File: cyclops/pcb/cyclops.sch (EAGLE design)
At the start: 178 parts, among them Q4 IRF510, U1 MCP4921, U11 THS4281, U12 MAX4564, U13 ZXTD, U14 ZXTD, U15 OPA1664, U2 LT1931, U3 LT1764A, U31 TPS62153, U4 BD00IA5WEFJ-E2, U5 TPS72325, U6 LT1711, U7 TLV3701, U8 ADR03, U9 LT1880

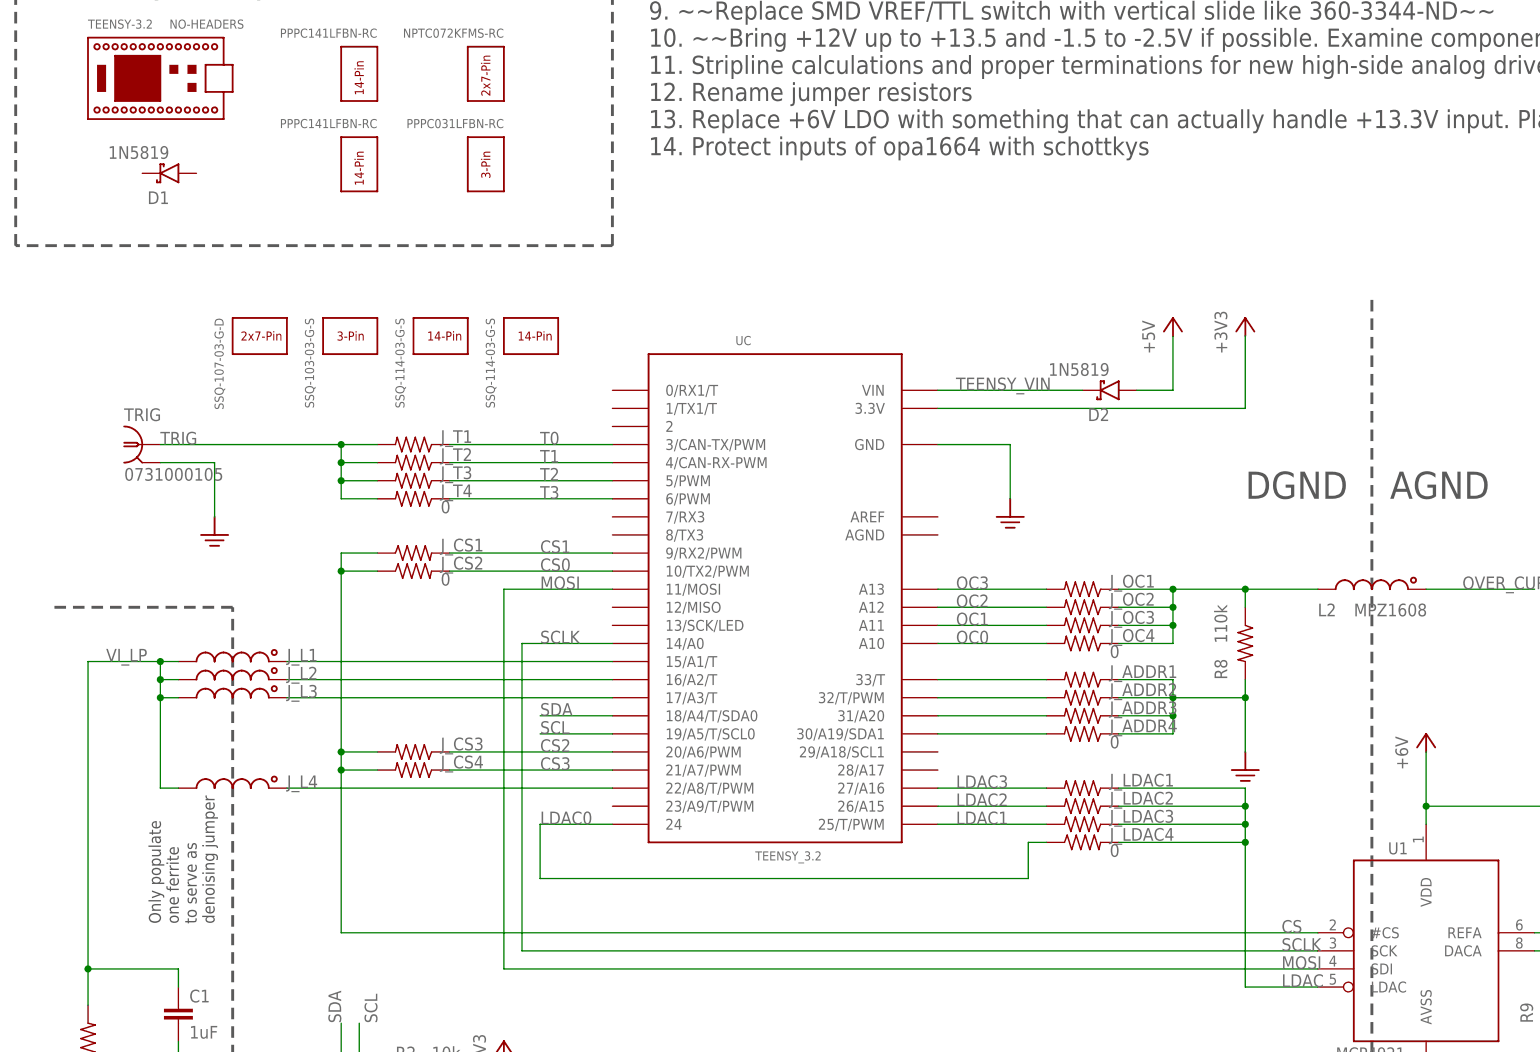
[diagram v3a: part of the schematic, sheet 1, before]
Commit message: Most digital layout is complete.
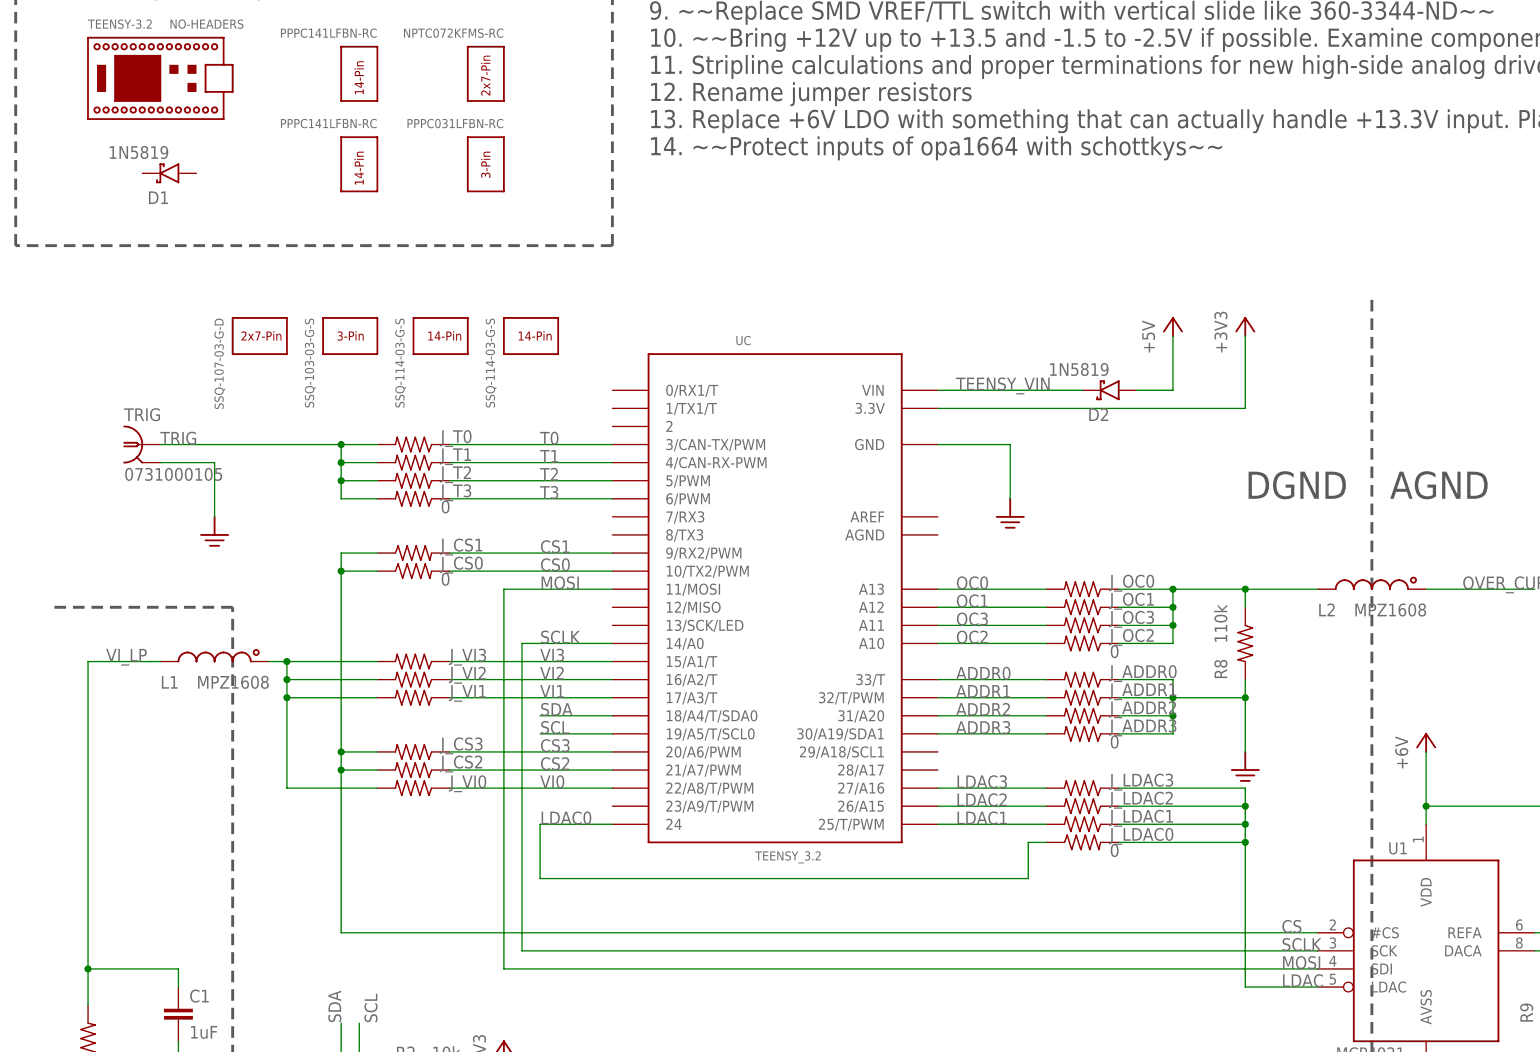
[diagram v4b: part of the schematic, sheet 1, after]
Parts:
- removed J_ADDR4, J_CS4, J_OC4, J_T4: 0, jonnew:R_0402
- removed J_L1, J_L2, J_L3, J_L4: MPZ1608, cyclops:L_0603
- added J_ADDR0, J_CS0, J_OC0, J_T0, J_VI0, J_VI1, J_VI2, J_VI3: 0, jonnew:R_0402
- added L1: MPZ1608, cyclops:L_0603
- renumbered J_LDAC4 to J_LDAC0
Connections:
- removed net N$19: J_L3.1, UC.17/A3/T
- removed net N$21: J_L2.1, UC.16/A2/T
- removed net N$23: J_L1.1, UC.15/A1/T
- removed net N$40: J_ADDR1.2, UC.33/T
- removed net N$41: J_ADDR2.2, UC.32/T/PWM
- removed net N$44: J_ADDR3.2, UC.31/A20
- removed net N$45: J_ADDR4.2, UC.30/A19/SDA1
- removed net N$7: J_L4.1, UC.22/A8/T/PWM
- new net ADDR0: J_ADDR0.2, UC.33/T
- new net ADDR1: J_ADDR1.2, UC.32/T/PWM
- new net ADDR2: J_ADDR2.2, UC.31/A20
- new net ADDR3: J_ADDR3.2, UC.30/A19/SDA1
- new net N$58: J_VI0.2, J_VI1.2, J_VI2.2, J_VI3.2, L1.1
- new net VI0: J_VI0.1, UC.22/A8/T/PWM
- new net VI1: J_VI1.1, UC.17/A3/T
- new net VI2: J_VI2.1, UC.16/A2/T
- new net VI3: J_VI3.1, UC.15/A1/T
- net CS: now also J_CS0.1, J_CS2.2; no longer J_CS2.1, J_CS4.2
- net CS0: now also J_CS0.2; no longer J_CS2.2
- net CS2: now also J_CS2.1, UC.21/A7/PWM; no longer J_CS3.1, UC.20/A6/PWM
- net CS3: now also J_CS3.1, UC.20/A6/PWM; no longer J_CS4.1, UC.21/A7/PWM
- net GND: now also J_ADDR0.1; no longer J_ADDR4.1
- net LDAC1: now also J_LDAC1.2; no longer J_LDAC3.2
- net LDAC3: now also J_LDAC3.2; no longer J_LDAC1.2
- net N$38: now also J_OC0.1; no longer J_OC4.1
- net OC0: now also J_OC0.2, UC.A13; no longer J_OC4.2, UC.A10
- net OC1: now also J_OC1.2, UC.A12; no longer J_OC3.2, UC.A11
- net OC2: now also UC.A10; no longer UC.A12
- net OC3: now also J_OC3.2, UC.A11; no longer J_OC1.2, UC.A13
- net OVER_CURR: now also U10.IN
- net T0: now also J_T0.1; no longer J_T1.1
- net T1: now also J_T1.1; no longer J_T2.1
- net T2: now also J_T2.1; no longer J_T3.1
- net T3: now also J_T3.1; no longer J_T4.1
- net TRIG: now also J_T0.2; no longer J_T4.2
- net VI_LP: now also L1.2; no longer J_L1.2, J_L2.2, J_L3.2, J_L4.2
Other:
- note removed: "Only populate one ferrite to serve as denoising jumper"
- moved on the sheet: J_ADDR1, J_ADDR2, J_ADDR3, J_CS2, J_LDAC1, J_LDAC3, J_OC1, J_OC2, J_T1, J_T2, J_T3

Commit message: Almost done with layout.
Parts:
- R10: device jonnew:R_0805 -> jonnew:R_0603
- R15: value 3k -> 2.2k
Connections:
- removed net N$38: J_OC0.1, J_OC1.1, J_OC2.1, J_OC3.1, L2.2, R8.1
- removed net V-: R20.2, U7G$2.V-, U9G$2.V-
- new net OVER_CURR_PRE: J_OC0.1, J_OC1.1, J_OC2.1, J_OC3.1, L2.2, R28.2, R8.1
- net GND: now also R20.2, U7G$2.V-, U9G$2.V-
- net OVER_CURR: no longer R28.2
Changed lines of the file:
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@@
 <part name="REF2V5" library="cyclops" deviceset="TP" device="TP16R" value="TPTP16R"/>
 <part name="REF5V0" library="cyclops" deviceset="TP" device="TP16R" value="TPTP16R"/>
-<part name="R15" library="cyclops" deviceset="R" device="_0603" value="3k"/>
+<part name="R15" library="cyclops" deviceset="R" device="_0603" value="2.2k"/>
 <part name="R20" library="cyclops" deviceset="R" device="_0603" value="10k"/>
 <part name="R17" library="cyclops" deviceset="R" device="_0603" value="40k"/>
@@
 <part name="U14" library="cyclops" deviceset="ZXTD4591E6" device="" value="ZXTD"/>
 <part name="SUPPLY14" library="cyclops" deviceset="+12V" device=""/>
-<part name="R10" library="jonnew" deviceset="R" device="_0805" value="100"/>
+<part name="R10" library="jonnew" deviceset="R" device="_0603" value="100"/>
 <part name="D3" library="cyclops" deviceset="Z-DIODE" device="_SOD-323" value="MM3Z5V1"/>
 <part name="U$21" library="cyclops" deviceset="GND2" device=""/>
@@
 </segment>
 </net>
-<net name="N$38" class="0">
+<net name="OVER_CURR_PRE" class="0">
 <segment>
 <wire x1="149.86" y1="101.6" x2="160.02" y2="101.6" width="0.1524" layer="91"/>
@@
 <wire x1="-43.18" y1="-45.72" x2="-43.18" y2="-48.26" width="0.1524" layer="91"/>
 </segment>
+<segment>
+<pinref part="U7" gate="G$2" pin="V-"/>
+<wire x1="-33.02" y1="60.96" x2="-33.02" y2="58.42" width="0.1524" layer="91"/>
+<pinref part="R20" gate="R" pin="2"/>
+<wire x1="-53.34" y1="58.42" x2="-53.34" y2="40.64" width="0.1524" layer="91"/>
+<wire x1="-33.02" y1="58.42" x2="-53.34" y2="58.42" width="0.1524" layer="91"/>
+<junction x="-53.34" y="58.42"/>
+<wire x1="-58.42" y1="58.42" x2="-53.34" y2="58.42" width="0.1524" layer="91"/>
+</segment>
 </net>
 <net name="N$5" class="0">
@@
 <wire x1="81.28" y1="93.98" x2="81.28" y2="88.9" width="0.1524" layer="91"/>
 <pinref part="OC" gate="2" pin="A"/>
-</segment>
-</net>
-<net name="OVER_CURR" class="0">
-<segment>
-<pinref part="R28" gate="R" pin="2"/>
-<wire x1="38.1" y1="68.58" x2="58.42" y2="68.58" width="0.1524" layer="91"/>
-<label x="38.1" y="68.58" size="1.778" layer="95"/>
 </segment>
 </net>
@@
 </segment>
 </net>
-<net name="V-" class="0">
-<segment>
-<pinref part="U7" gate="G$2" pin="V-"/>
-<wire x1="-33.02" y1="60.96" x2="-33.02" y2="58.42" width="0.1524" layer="91"/>
-<pinref part="R20" gate="R" pin="2"/>
-<wire x1="-53.34" y1="58.42" x2="-53.34" y2="40.64" width="0.1524" layer="91"/>
-<wire x1="-33.02" y1="58.42" x2="-53.34" y2="58.42" width="0.1524" layer="91"/>
-<junction x="-53.34" y="58.42"/>
-<wire x1="-58.42" y1="58.42" x2="-53.34" y2="58.42" width="0.1524" layer="91"/>
-</segment>
-</net>
 <net name="-2.5V" class="0">
 <segment>
@@
 <wire x1="-96.52" y1="58.42" x2="-116.84" y2="58.42" width="0.1524" layer="91"/>
 <label x="-116.84" y="58.42" size="1.778" layer="95"/>
+</segment>
+</net>
+<net name="OVER_CURR_PRE" class="0">
+<segment>
+<pinref part="R28" gate="R" pin="2"/>
+<wire x1="38.1" y1="68.58" x2="58.42" y2="68.58" width="0.1524" layer="91"/>
+<label x="38.1" y="68.58" size="1.778" layer="95"/>
 </segment>
 </net>
@@
 <wire x1="53.34" y1="-33.02" x2="53.34" y2="-73.66" width="0.1524" layer="91"/>
 </segment>
+<segment>
+<pinref part="U9" gate="G$2" pin="V-"/>
+<wire x1="5.08" y1="-35.56" x2="5.08" y2="-27.94" width="0.1524" layer="91"/>
+</segment>
 </net>
 <net name="N$6" class="0">
@@
 </segment>
 </net>
-<net name="V-" class="0">
-<segment>
-<pinref part="U9" gate="G$2" pin="V-"/>
-<wire x1="5.08" y1="-35.56" x2="5.08" y2="-27.94" width="0.1524" layer="91"/>
-</segment>
-</net>

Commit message: More routing. Very near completion.
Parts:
- removed C40: 10uF, jonnew:C_1206
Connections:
- net N$50 renamed ~LED_ACTIVE
- removed net N$48: D6.A
- removed net N$53: D5.C
- net +13.3V: no longer C40.1
- net +6V: now also D5.C
- net GND: now also D6.A; no longer C40.2
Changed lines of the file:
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@@
 <part name="U$2" library="cyclops" deviceset="GND2" device=""/>
 <part name="P+18" library="jonnew" deviceset="+5V" device="" value="+5V"/>
-<part name="C40" library="jonnew" deviceset="C" device="_1206" value="10uF"/>
 <part name="U31" library="jonnew" deviceset="TPS6125X" device="_VQFN16" value="TPS62153"/>
 <part name="L5" library="jonnew" deviceset="L" device="_4020" value="XFL4020-222ME"/>
@@
 <junction x="160.02" y="86.36"/>
 </segment>
+<segment>
+<pinref part="D6" gate="G$1" pin="A"/>
+<wire x1="20.32" y1="-63.5" x2="20.32" y2="-60.96" width="0.1524" layer="91"/>
+</segment>
 </net>
 <net name="VAUX" class="0">
@@
 <pinref part="C5" gate="C" pin="1"/>
 <wire x1="251.46" y1="71.12" x2="251.46" y2="45.72" width="0.1524" layer="91"/>
+</segment>
+<segment>
+<pinref part="D5" gate="G$1" pin="C"/>
+<wire x1="20.32" y1="-40.64" x2="20.32" y2="-38.1" width="0.1524" layer="91"/>
 </segment>
 </net>
@@
 <pinref part="R7" gate="R" pin="1"/>
 <wire x1="99.06" y1="-50.8" x2="101.6" y2="-50.8" width="0.1524" layer="91"/>
-</segment>
-</net>
-<net name="N$48" class="0">
-<segment>
-<pinref part="D6" gate="G$1" pin="A"/>
-<wire x1="20.32" y1="-63.5" x2="20.32" y2="-60.96" width="0.1524" layer="91"/>
-</segment>
-</net>
-<net name="N$53" class="0">
-<segment>
-<pinref part="D5" gate="G$1" pin="C"/>
-<wire x1="20.32" y1="-40.64" x2="20.32" y2="-38.1" width="0.1524" layer="91"/>
 </segment>
 </net>
@@
 <instance part="U4" gate="G$1" x="86.36" y="30.48"/>
 <instance part="P+18" gate="1" x="40.64" y="-33.02"/>
-<instance part="C40" gate="C" x="17.78" y="30.48"/>
 <instance part="U31" gate="G$1" x="-25.4" y="-50.8"/>
 <instance part="L5" gate="L" x="0" y="-38.1" rot="R270"/>
@@
 <pinref part="C10" gate="C" pin="-"/>
 <wire x1="-38.1" y1="-2.54" x2="-38.1" y2="-10.16" width="0.1524" layer="91"/>
-<pinref part="C40" gate="C" pin="2"/>
-<wire x1="17.78" y1="25.4" x2="17.78" y2="-2.54" width="0.1524" layer="91"/>
-<wire x1="17.78" y1="-2.54" x2="7.62" y2="-2.54" width="0.1524" layer="91"/>
-<junction x="7.62" y="-2.54"/>
 </segment>
 <segment>
@@
 <wire x1="27.94" y1="22.86" x2="27.94" y2="38.1" width="0.1524" layer="91"/>
 <junction x="7.62" y="38.1"/>
-<wire x1="7.62" y1="38.1" x2="17.78" y2="38.1" width="0.1524" layer="91"/>
-<wire x1="17.78" y1="38.1" x2="27.94" y2="38.1" width="0.1524" layer="91"/>
+<wire x1="7.62" y1="38.1" x2="27.94" y2="38.1" width="0.1524" layer="91"/>
 <wire x1="27.94" y1="38.1" x2="27.94" y2="45.72" width="0.1524" layer="91"/>
 <junction x="27.94" y="38.1"/>
 <pinref part="SUPPLY9" gate="G$1" pin="+12V"/>
-<pinref part="C40" gate="C" pin="1"/>
-<wire x1="17.78" y1="38.1" x2="17.78" y2="33.02" width="0.1524" layer="91"/>
-<junction x="17.78" y="38.1"/>
 <pinref part="C12" gate="C" pin="1"/>
 <pinref part="U4" gate="G$1" pin="EN"/>
@@
 </segment>
 </net>
-<net name="N$50" class="0">
+<net name="~LED_ACTIVE" class="0">
 <segment>
 <wire x1="-10.16" y1="-27.94" x2="-10.16" y2="-2.54" width="0.1524" layer="91"/>
@@
 <pinref part="U6" gate="G$1" pin="Q"/>
 <wire x1="-27.94" y1="-27.94" x2="-10.16" y2="-27.94" width="0.1524" layer="91"/>
-</segment>
-</net>
+<label x="-7.62" y="-27.94" size="1.778" layer="95" rot="R90"/>
+</segment>
+</net>

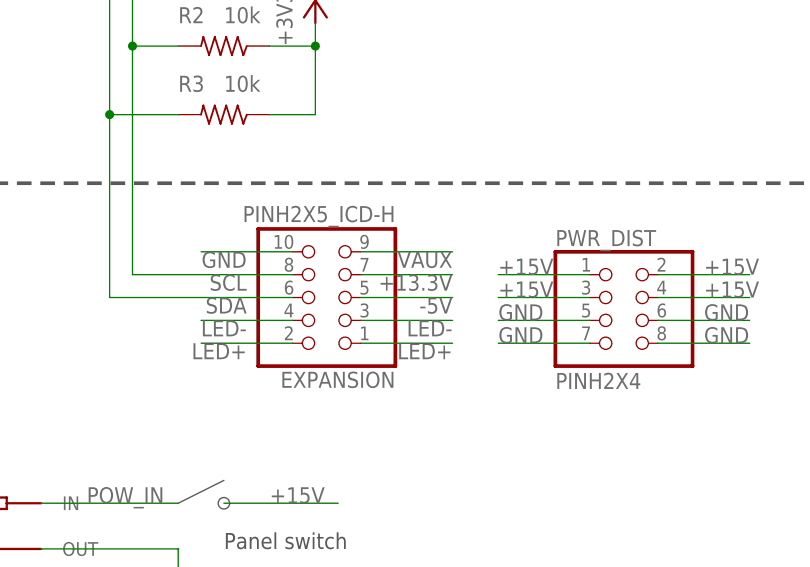
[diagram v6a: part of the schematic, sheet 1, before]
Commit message: More routing. Need to do ERC/DRC at this point.
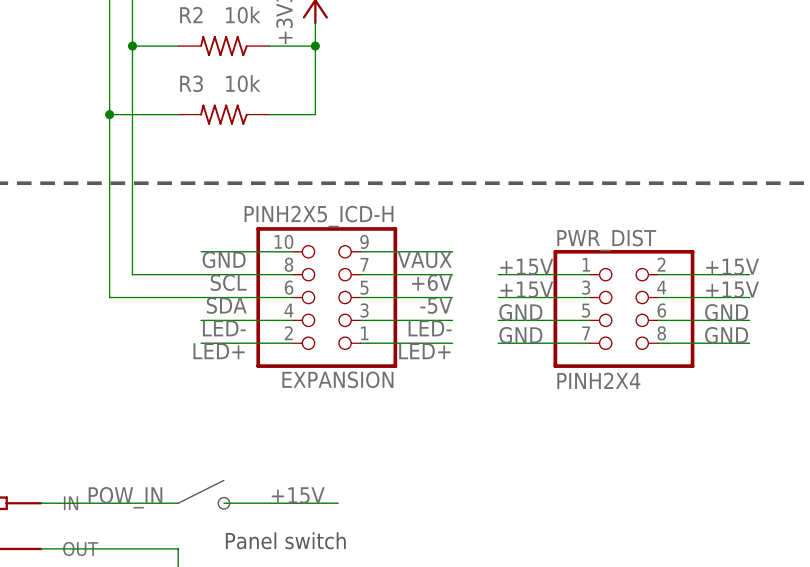
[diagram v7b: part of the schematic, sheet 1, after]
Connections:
- net +13.3V: no longer EXPANSION.7
- net +6V: now also EXPANSION.7
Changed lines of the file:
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@@
-</segment>
-</net>
-<net name="+13.3V" class="1">
-<segment>
-<pinref part="EXPANSION" gate="G$1" pin="7"/>
-<wire x1="60.96" y1="7.62" x2="71.12" y2="7.62" width="0.1524" layer="91"/>
-<label x="71.12" y="7.62" size="1.778" layer="95" rot="R180"/>
 </segment>
 </net>
@@
 <wire x1="20.32" y1="-40.64" x2="20.32" y2="-38.1" width="0.1524" layer="91"/>
 </segment>
-</net>
+<segment>
+<pinref part="EXPANSION" gate="G$1" pin="7"/>
+<wire x1="60.96" y1="7.62" x2="71.12" y2="7.62" width="0.1524" layer="91"/>
+<label x="71.12" y="7.62" size="1.778" layer="95" rot="R180"/>
+</segment>
+</net>
